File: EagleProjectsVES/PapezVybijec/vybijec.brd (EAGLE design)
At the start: 55.9 x 40.9 mm, 32 parts, among them P1 COLLECTOR, P2 BASE, P3 EMITTER, P4 GROUND, P5 COL, P6 EMIT

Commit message: gitignore: - pridany knihovny
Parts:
- added LED1: (no value), adafruit:LED3MM
- added R14: 1R0, rcl:0207/10
- IO1: value (none) -> NCS2001SN2T1G
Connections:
- new net N$12: LED1.K, R14.2
- net GND: now also R14.1
- net VCC: now also LED1.A
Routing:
- net GND: track 11.7 -> 39.9 mm
- net N$12: track 0.00 -> 2.54 mm
- net VCC: track 37.8 -> 40.0 mm

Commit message: PapezVybijec: - opraveny rozmery nytu
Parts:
- P5, P6: device PADs:PAD3MM -> PADs:PAD1.6MM
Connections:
- net N$10: now also P5.P$1; no longer P5.1
- net N$11: now also P6.P$1; no longer P6.1
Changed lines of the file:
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@@
 <attribute name="DIAMETER" value="3mm" x="52.07" y="11.43" size="1.778" layer="27" display="off"/>
 </element>
-<element name="P5" library="PADs" package="PAD3MM" value="COL" x="33.02" y="3.175" rot="R270">
-<attribute name="DIAMETER" value="3mm" x="33.02" y="3.175" size="1.778" layer="27" rot="R270" display="off"/>
-</element>
-<element name="P6" library="PADs" package="PAD3MM" value="EMIT" x="27.94" y="3.175" rot="R270">
-<attribute name="DIAMETER" value="3mm" x="27.94" y="3.175" size="1.778" layer="27" rot="R270" display="off"/>
-</element>
+<element name="P5" library="PADs" package="PAD1.6MM" value="COL" x="33.02" y="3.175" rot="R270"/>
+<element name="P6" library="PADs" package="PAD1.6MM" value="EMIT" x="27.94" y="3.175" rot="R270"/>
 <element name="R1" library="rcl" package="0207/10" value="M33" x="22.86" y="30.48"/>
 <element name="R10" library="rcl" package="0207/10" value="15k" x="34.29" y="19.05"/>
@@
 </signal>
 <signal name="N$10">
-<contactref element="P5" pad="1"/>
+<contactref element="P5" pad="P$1"/>
 <contactref element="OK1" pad="5"/>
 <wire x1="33.02" y1="3.175" x2="33.02" y2="7.62" width="1.016" layer="16"/>
 </signal>
 <signal name="N$11">
-<contactref element="P6" pad="1"/>
+<contactref element="P6" pad="P$1"/>
 <contactref element="OK1" pad="4"/>
 <wire x1="30.48" y1="7.62" x2="30.48" y2="5.715" width="1.016" layer="16"/>

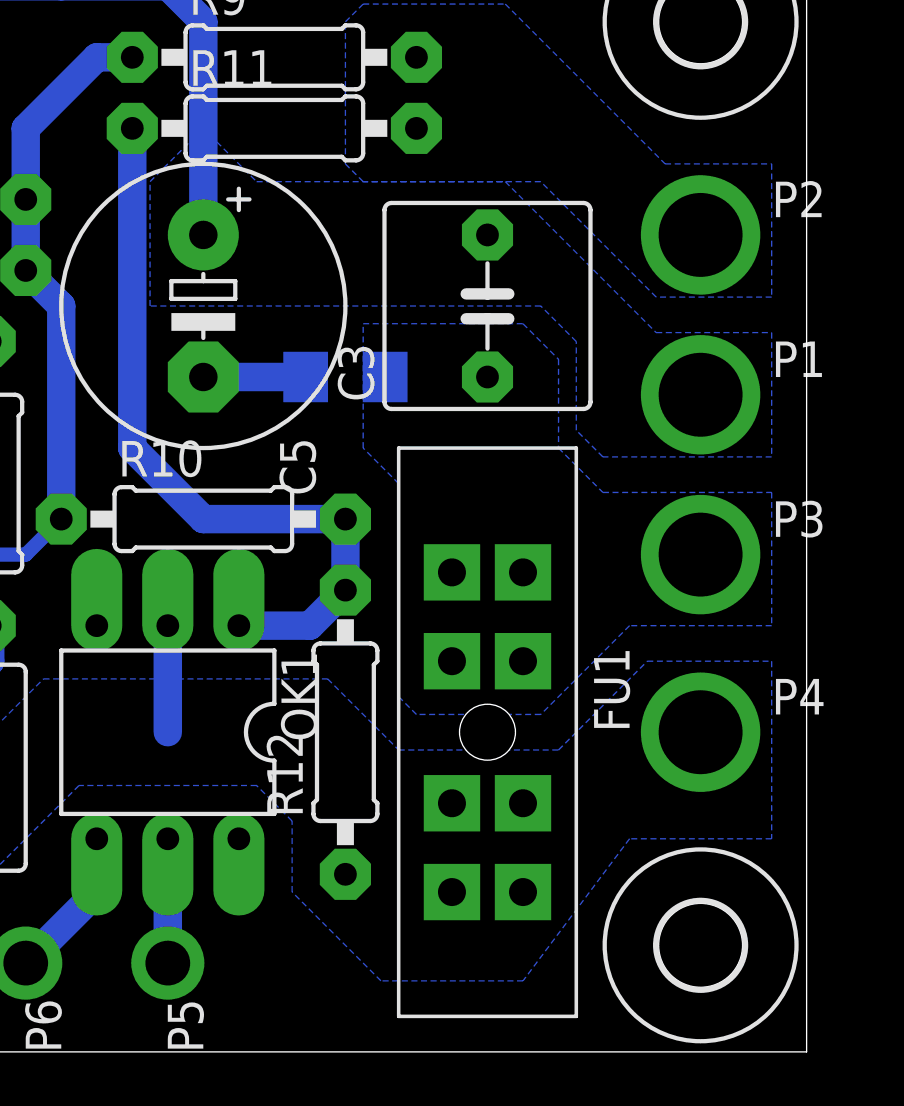
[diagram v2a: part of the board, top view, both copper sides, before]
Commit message: PapezVybijec: - hotove podklady, - pridany navrhove pravidla
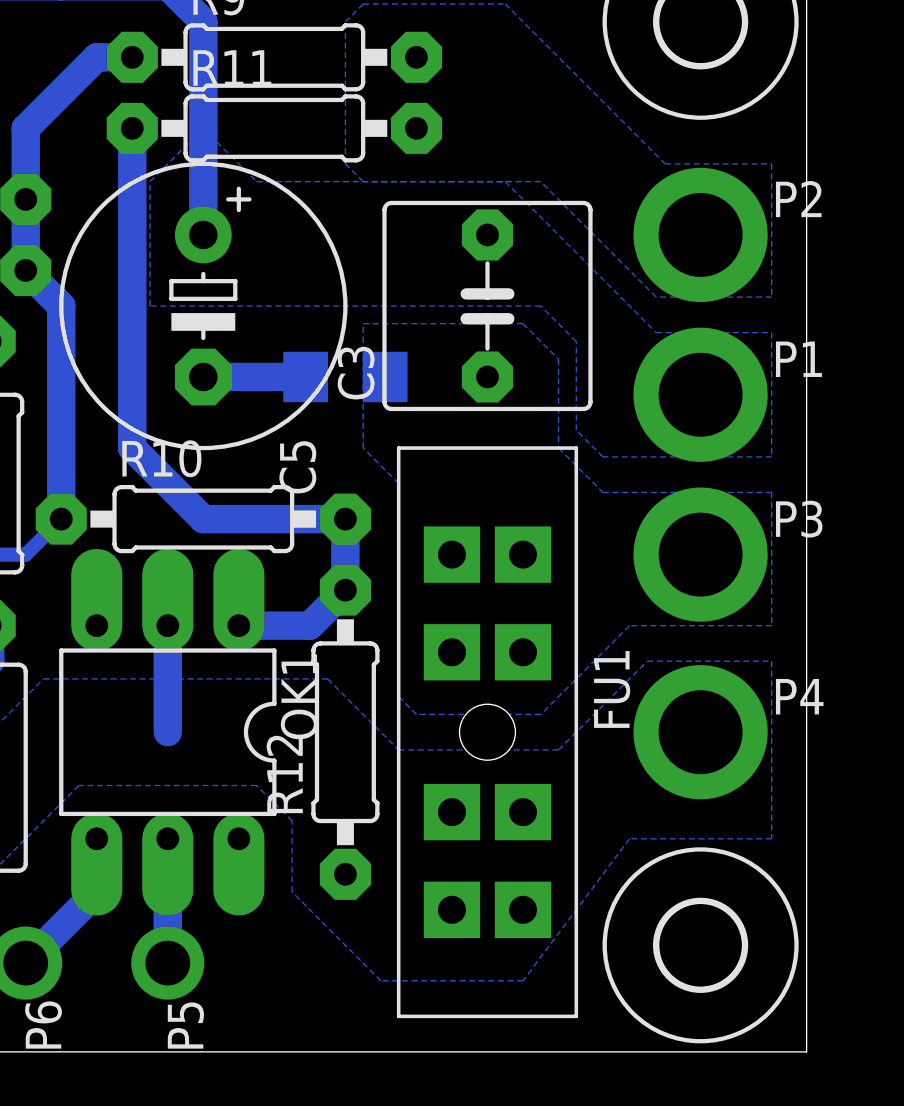
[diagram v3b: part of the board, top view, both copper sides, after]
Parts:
- R14: value 1R0 -> 330R
